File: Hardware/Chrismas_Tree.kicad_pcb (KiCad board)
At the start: 2 copper layers, 264.4 x 368.3 mm, 213 parts, among them J1 DNP, J2 USB_B, Q1 2N2222A, Q2 2N2222A, Q3 2N2222A, Q4 2N2222A, U1 PIC18F23K22

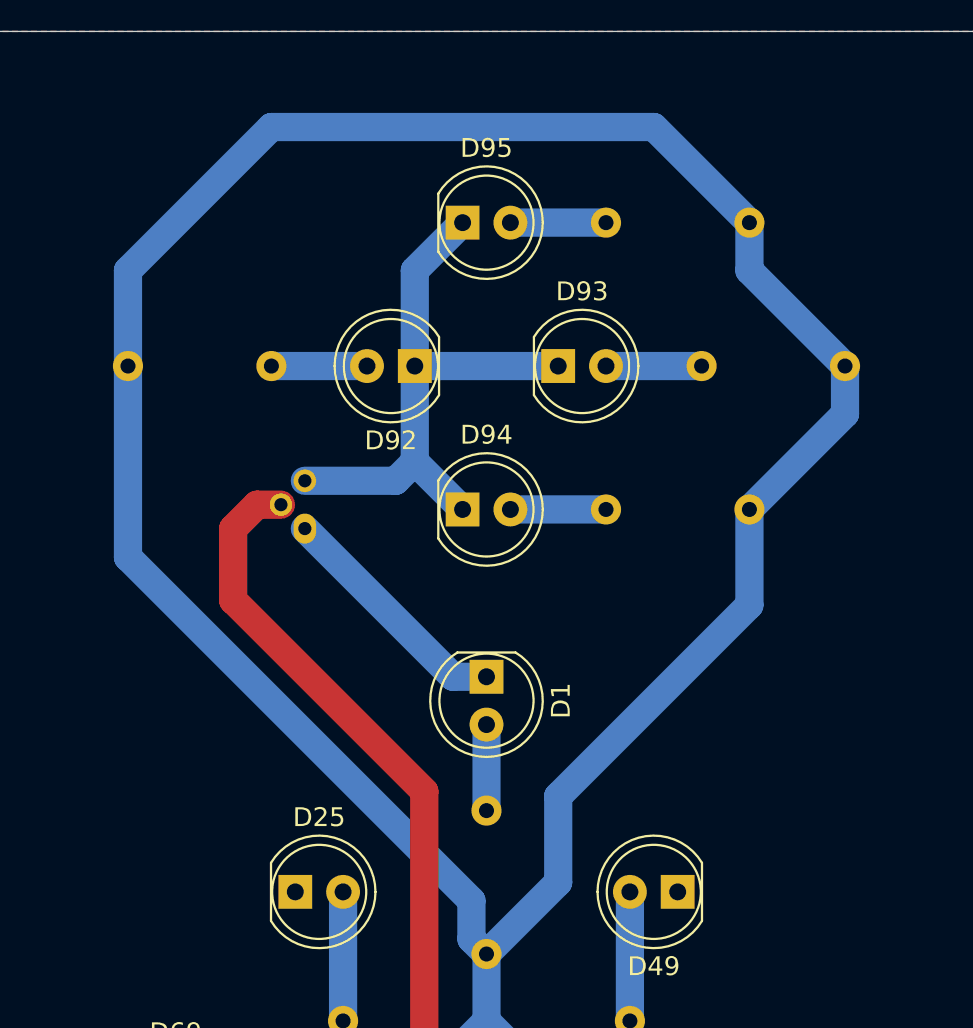
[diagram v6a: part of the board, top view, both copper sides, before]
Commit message: Replaced light bulb through-hole resistors by SMD ones.
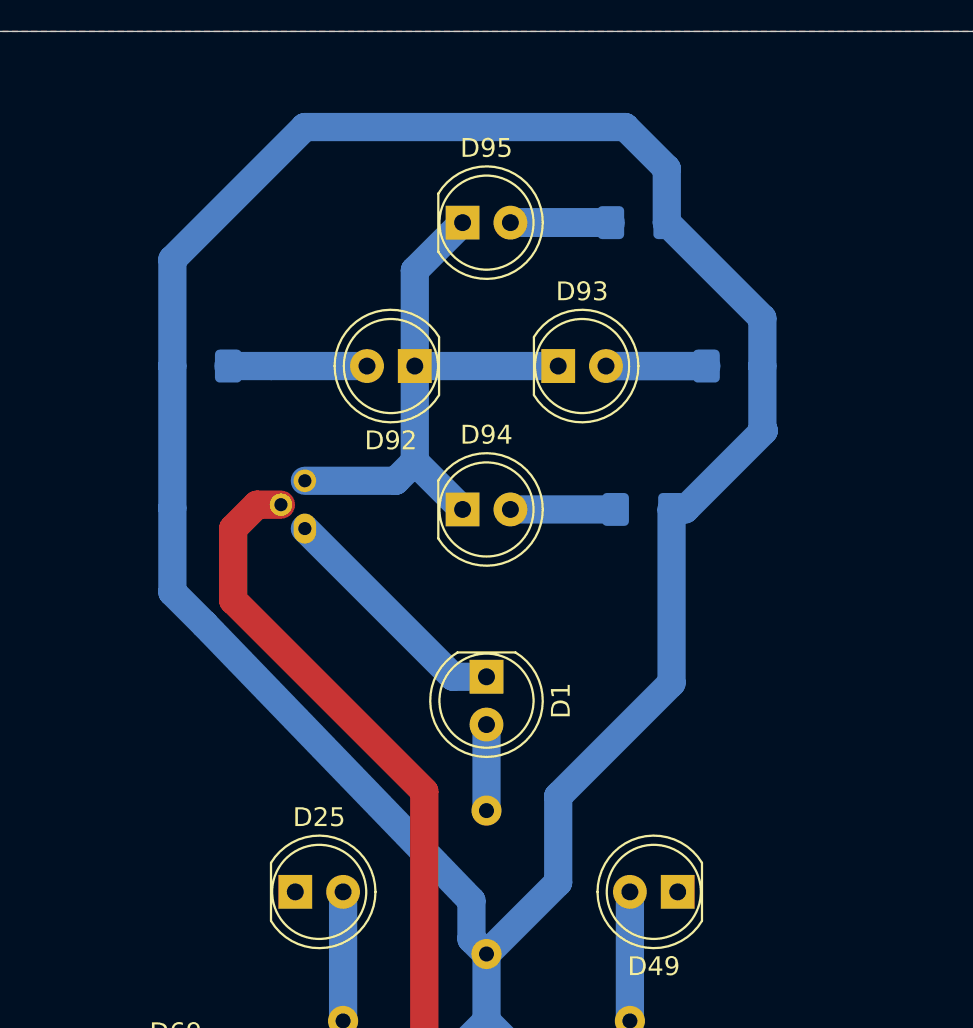
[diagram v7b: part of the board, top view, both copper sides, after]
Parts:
- R92, R93, R94, R95: footprint Resistor_THT:R_Axial_DIN0207_L6.3mm_D2.5mm_P7.62mm_Horizontal -> Resistor_SMD:R_1206_3216Metric_Pad1.42x1.75mm_HandSolder
- moved R93 5.88 mm to (175.2, 43.4)
- moved R95 5.88 mm to (170.1, 35.8)
- moved R94 5.62 mm to (170.4, 51.1)
- moved R92 3.85 mm to (146.8, 43.4)
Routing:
- net +5V: track 1791.3 -> 1784.1 mm
- net Net-(D95-Pad2): track 5.08 -> 10.4 mm
- net Net-(D93-Pad2): track 5.08 -> 10.4 mm
- net Net-(D92-Pad2): track 5.08 -> 7.37 mm

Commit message: Put all amber leds in their right place.
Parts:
- moved D44 267.5 mm to (179.8, 82.8), turned to 180 degrees
- moved D70 267.5 mm to (137.4, 347.0), turned to 0 degrees
- moved D21 263.8 mm to (198.9, 101.9), turned to 180 degrees
- moved D71 263.8 mm to (137.4, 358.4), turned to 0 degrees
- moved D22 260.1 mm to (198.9, 118.4), turned to 180 degrees
- moved D72 260.1 mm to (137.4, 371.1), turned to 0 degrees
- moved R21 256.6 mm to (183.6, 103.6), turned to 0 degrees
- moved R71 256.6 mm to (153.2, 358.4), turned to 180 degrees
- moved R22 256.4 mm to (190.0, 110.7)
- moved R72 256.4 mm to (146.8, 363.5)
- moved D23 253.4 mm to (187.5, 134.9), turned to 180 degrees
- moved D73 253.4 mm to (137.4, 383.3), turned to 0 degrees
- moved D67 252.8 mm to (144.3, 82.8)
- moved D69 252.8 mm to (137.4, 335.5)
- moved R44 250.6 mm to (177.3, 97.5), turned to 90 degrees
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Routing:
- net Net-(D77-Pad2): track 4.57 -> 8.27 mm
- net Net-(D46-Pad2): track 8.27 -> 4.57 mm
- net Net-(D75-Pad2): track 8.21 -> 4.57 mm
- net Net-(D48-Pad2): track 4.57 -> 8.21 mm
- net Net-(D73-Pad2): track 5.08 -> 8.37 mm
- net Net-(D23-Pad2): track 8.37 -> 5.08 mm
- net Net-(D76-Pad2): track 5.08 -> 6.97 mm
- net Net-(D47-Pad2): track 6.97 -> 5.08 mm
- net Net-(D74-Pad2): track 5.08 -> 6.97 mm
- net Net-(D24-Pad2): track 6.97 -> 5.08 mm
- net Net-(D70-Pad2): track 7.11 -> 5.59 mm
- net Net-(D44-Pad2): track 5.59 -> 7.11 mm
- net Net-(D78-Pad2): track 5.75 -> 6.60 mm
- net Net-(D45-Pad2): track 6.60 -> 5.75 mm
- net Net-(D80-Pad2): track 6.10 -> 5.33 mm
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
